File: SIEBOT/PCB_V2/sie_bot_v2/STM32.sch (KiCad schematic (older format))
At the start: 23 parts, among them U10 STM32F105RC, X3 8 MHz

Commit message: Adición de programadores con ejemplos de manejo de los diferentes periféricos
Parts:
- removed X3: 8 MHz, symbol CRYSTAL
- added X3: 8MHz, ABM8G, symbol ABM8G
- C26, C28, C33, C55, C58, C72, D10, D8, D9, R26, R27, R33, R34, R35, R5: footprint (none) -> SM0603
- C54, C73: footprint (none) -> SM0805
- C56: value 1uF -> 0.1uF; footprint (none) -> SM0603
- C59: footprint (none) -> SM1206
- U10: footprint lqfp64 -> TQFP_64
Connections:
- net labels removed: STM32_FP[0..40]
- wire segments 112 -> 116
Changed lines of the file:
@@
-EESchema Schematic File Version 2  date Tue 20 Sep 2011 03:35:58 PM COT
+EESchema Schematic File Version 2  date Wed 21 Sep 2011 02:34:46 PM COT
 LIBS:con-jack
 LIBS:adm3101e
@@
 Sheet 2 5
 Title ""
-Date "20 sep 2011"
+Date "21 sep 2011"
 Rev ""
 Comp ""
@@
 Comment4 ""
 $EndDescr
-Text Label 6000 2300 0    60   ~ 0
-STM32_FP42
-Text Label 6000 2200 0    60   ~ 0
-STM32_FP41
+Wire Wire Line
+	1000 2050 1000 2300
+Wire Wire Line
+	1000 2050 1150 2050
 Wire Bus Line
 	6750 4600 6750 2300
@@
 Wire Wire Line
 	6650 4400 5750 4400
+Wire Wire Line
+	1150 1950 1000 1950
+Wire Wire Line
+	1000 1950 1000 1700
+$Comp
+L ABM8G X3
+U 1 1 4E7A2D7B
+P 1550 2000
+F 0 "X3" H 1550 2150 60  0000 C CNN
+F 1 "8MHz" H 1550 1850 60  0000 C CNN
+F 2 "ABM8G" H 1550 2000 60  0001 C CNN
+	1    1550 2000
+	0    1    1    0
+$EndComp
+Text Label 6000 2300 0    60   ~ 0
+STM32_FP42
+Text Label 6000 2200 0    60   ~ 0
+STM32_FP41
 Entry Wire Line
 	6650 2200 6750 2300
@@
 F 0 "R27" V 9580 4550 50  0000 C CNN
 F 1 "10k" V 9500 4550 50  0000 C CNN
+F 2 "SM0603" H 9500 4550 60  0001 C CNN
 	1    9500 4550
 	-1   0    0    1
@@
 El procesador selecciona si inicia por \nla flash o ram internas.\nSe debe soldar solo R26 o R34\n\n
 $Comp
-L GND #PWR13
+L GND #PWR01
 U 1 1 4E78C5F4
 P 10450 4900
-F 0 "#PWR13" H 10450 4900 30  0001 C CNN
+F 0 "#PWR01" H 10450 4900 30  0001 C CNN
 F 1 "GND" H 10450 4830 30  0001 C CNN
 	1    10450 4900
@@
 F 0 "R26" V 9930 4550 50  0000 C CNN
 F 1 "510" V 9850 4550 50  0000 C CNN
+F 2 "SM0603" H 9850 4550 60  0001 C CNN
 	1    9850 4550
 	-1   0    0    1
@@
 F 0 "R34" V 10530 4550 50  0000 C CNN
 F 1 "10k" V 10450 4550 50  0000 C CNN
+F 2 "SM0603" H 10450 4550 60  0001 C CNN
 	1    10450 4550
 	-1   0    0    1
@@
 $EndComp
 $Comp
-L GND #PWR5
+L GND #PWR02
 U 1 1 4E78C2ED
 P 5300 7400
-F 0 "#PWR5" H 5300 7400 30  0001 C CNN
+F 0 "#PWR02" H 5300 7400 30  0001 C CNN
 F 1 "GND" H 5300 7330 30  0001 C CNN
 	1    5300 7400
@@
 F 0 "C59" H 10450 2550 50  0000 L CNN
 F 1 "10uF Tant." H 10450 2350 50  0000 L CNN
+F 2 "SM1206" H 10400 2450 60  0001 C CNN
 	1    10400 2450
 	1    0    0    -1
@@
 STM32_FP17
 $Comp
-L GND #PWR16
+L GND #PWR03
 U 1 1 4E188E68
 P 10950 1500
-F 0 "#PWR16" H 10950 1500 30  0001 C CNN
+F 0 "#PWR03" H 10950 1500 30  0001 C CNN
 F 1 "GND" H 10950 1430 30  0001 C CNN
 	1    10950 1500
@@
 F 0 "D10" H 10550 1300 50  0000 C CNN
 F 1 "LED" H 10550 1100 50  0000 C CNN
+F 2 "SM0603" H 10550 1200 60  0001 C CNN
 	1    10550 1200
 	-1   0    0    1
@@
 F 0 "R35" V 10630 1500 50  0000 C CNN
 F 1 "1k" V 10550 1500 50  0000 C CNN
+F 2 "SM0603" H 10550 1500 60  0001 C CNN
 	1    10550 1500
 	0    1    1    0
@@
 F 0 "R33" V 9780 1500 50  0000 C CNN
 F 1 "1k" V 9700 1500 50  0000 C CNN
+F 2 "SM0603" H 9700 1500 60  0001 C CNN
 	1    9700 1500
 	0    1    1    0
@@
 F 0 "D9" H 9700 1300 50  0000 C CNN
 F 1 "LED" H 9700 1100 50  0000 C CNN
+F 2 "SM0603" H 9700 1200 60  0001 C CNN
 	1    9700 1200
 	-1   0    0    1
 $EndComp
 $Comp
-L GND #PWR11
+L GND #PWR04
 U 1 1 4E188E4E
 P 10100 1500
-F 0 "#PWR11" H 10100 1500 30  0001 C CNN
+F 0 "#PWR04" H 10100 1500 30  0001 C CNN
 F 1 "GND" H 10100 1430 30  0001 C CNN
 	1    10100 1500
@@
 STM32_FP1
 $Comp
-L GND #PWR7
+L GND #PWR05
 U 1 1 4E186DEB
 P 9250 1500
-F 0 "#PWR7" H 9250 1500 30  0001 C CNN
+F 0 "#PWR05" H 9250 1500 30  0001 C CNN
 F 1 "GND" H 9250 1430 30  0001 C CNN
 	1    9250 1500
@@
 F 0 "U10" H 3200 8150 60  0000 C CNN
 F 1 "STM32F105RC" H 5100 2600 60  0000 C CNN
-F 2 "lqfp64" H 3140 8210 60  0001 C CNN
+F 2 "TQFP_64" H 3140 8210 60  0001 C CNN
 	1    4200 4800
 	1    0    0    -1
@@
 P 9700 2450
 F 0 "C56" H 9750 2550 50  0000 L CNN
-F 1 "1uF" H 9750 2350 50  0000 L CNN
+F 1 "0.1uF" H 9750 2350 50  0000 L CNN
+F 2 "SM0603" H 9700 2450 60  0001 C CNN
 	1    9700 2450
 	1    0    0    -1
@@
 F 0 "C54" H 9050 2550 50  0000 L CNN
 F 1 "1uF" H 9050 2350 50  0000 L CNN
+F 2 "SM0805" H 9000 2450 60  0001 C CNN
 	1    9000 2450
 	1    0    0    -1
 $EndComp
 $Comp
-L GND #PWR14
+L GND #PWR06
 U 1 1 4E07869F
 P 10600 2750
-F 0 "#PWR14" H 10600 2750 30  0001 C CNN
+F 0 "#PWR06" H 10600 2750 30  0001 C CNN
 F 1 "GND" H 10600 2680 30  0001 C CNN
 	1    10600 2750
@@
 $EndComp
 $Comp
-L GND #PWR3
+L GND #PWR07
 U 1 1 4DCDB18D
 P 4300 7400
-F 0 "#PWR3" H 4300 7400 30  0001 C CNN
+F 0 "#PWR07" H 4300 7400 30  0001 C CNN
 F 1 "GND" H 4300 7330 30  0001 C CNN
 	1    4300 7400
@@
 F 0 "C33" H 8700 2550 50  0000 L CNN
 F 1 "0.1uF" H 8700 2350 50  0000 L CNN
+F 2 "SM0603" H 8650 2450 60  0001 C CNN
 	1    8650 2450
 	1    0    0    -1
@@
 F 0 "C55" H 9400 2550 50  0000 L CNN
 F 1 "0.1uF" H 9400 2350 50  0000 L CNN
+F 2 "SM0603" H 9350 2450 60  0001 C CNN
 	1    9350 2450
 	1    0    0    -1
@@
 F 0 "C58" H 10100 2550 50  0000 L CNN
 F 1 "0.1uF" H 10100 2350 50  0000 L CNN
+F 2 "SM0603" H 10050 2450 60  0001 C CNN
 	1    10050 2450
 	1    0    0    -1
@@
 F 0 "C72" H 10450 3400 50  0000 L CNN
 F 1 "0.1uF" H 10450 3200 50  0000 L CNN
+F 2 "SM0603" H 10400 3300 60  0001 C CNN
 	1    10400 3300
 	1    0    0    -1
@@
 F 0 "C73" H 10850 3400 50  0000 L CNN
 F 1 "1uF" H 10850 3200 50  0000 L CNN
+F 2 "SM0805" H 10800 3300 60  0001 C CNN
 	1    10800 3300
 	1    0    0    -1
 $EndComp
 $Comp
-L GND #PWR15
+L GND #PWR08
 U 1 1 4DCDB183
 P 10600 3600
-F 0 "#PWR15" H 10600 3600 30  0001 C CNN
+F 0 "#PWR08" H 10600 3600 30  0001 C CNN
 F 1 "GND" H 10600 3530 30  0001 C CNN
 	1    10600 3600
@@
 NRST
 $Comp
-L GND #PWR1
+L GND #PWR09
 U 1 1 4DCDB180
 P 700 2050
-F 0 "#PWR1" H 700 2050 30  0001 C CNN
+F 0 "#PWR09" H 700 2050 30  0001 C CNN
 F 1 "GND" H 700 1980 30  0001 C CNN
 	1    700  2050
 	-1   0    0    -1
-$EndComp
-$Comp
-L CRYSTAL X3
-U 1 1 4DCDB17F
-P 1550 2000
-F 0 "X3" H 1650 2150 60  0000 C CNN
-F 1 "8 MHz" H 1550 1850 60  0000 C CNN
-	1    1550 2000
-	0    -1   1    0
 $EndComp
 Text Label 2500 1800 0    60   ~ 0
@@
 BOOT0
 $Comp
-L GND #PWR9
+L GND #PWR010
 U 1 1 4DCDB17D
 P 9500 4900
-F 0 "#PWR9" H 9500 4900 30  0001 C CNN
+F 0 "#PWR010" H 9500 4900 30  0001 C CNN
 F 1 "GND" H 9500 4830 30  0001 C CNN
 	1    9500 4900
@@
 	850  4050 950  4150
 Text HLabel 1400 4350 2    60   BiDi ~ 0
-STM32_FP[0..40]
+STM32_FP[0..42]
 Text Label 1000 2650 0    60   ~ 0
 STM32_FP0
@@
 F 0 "D8" H 8850 1300 50  0000 C CNN
 F 1 "LED" H 8850 1100 50  0000 C CNN
+F 2 "SM0603" H 8850 1200 60  0001 C CNN
 	1    8850 1200
 	-1   0    0    1
@@
 F 0 "R5" V 8930 1500 50  0000 C CNN
 F 1 "1k" V 8850 1500 50  0000 C CNN
+F 2 "SM0603" H 8850 1500 60  0001 C CNN
 	1    8850 1500
 	0    1    1    0
@@
 F 0 "C26" H 1250 1800 50  0000 L CNN
 F 1 "22pF" H 1250 1600 50  0000 L CNN
+F 2 "SM0603" H 1200 1700 60  0001 C CNN
 	1    1200 1700
 	0    1    1    0
@@
 F 0 "C28" H 1250 2400 50  0000 L CNN
 F 1 "22pF" H 1250 2200 50  0000 L CNN
+F 2 "SM0603" H 1200 2300 60  0001 C CNN
 	1    1200 2300
 	0    1    1    0

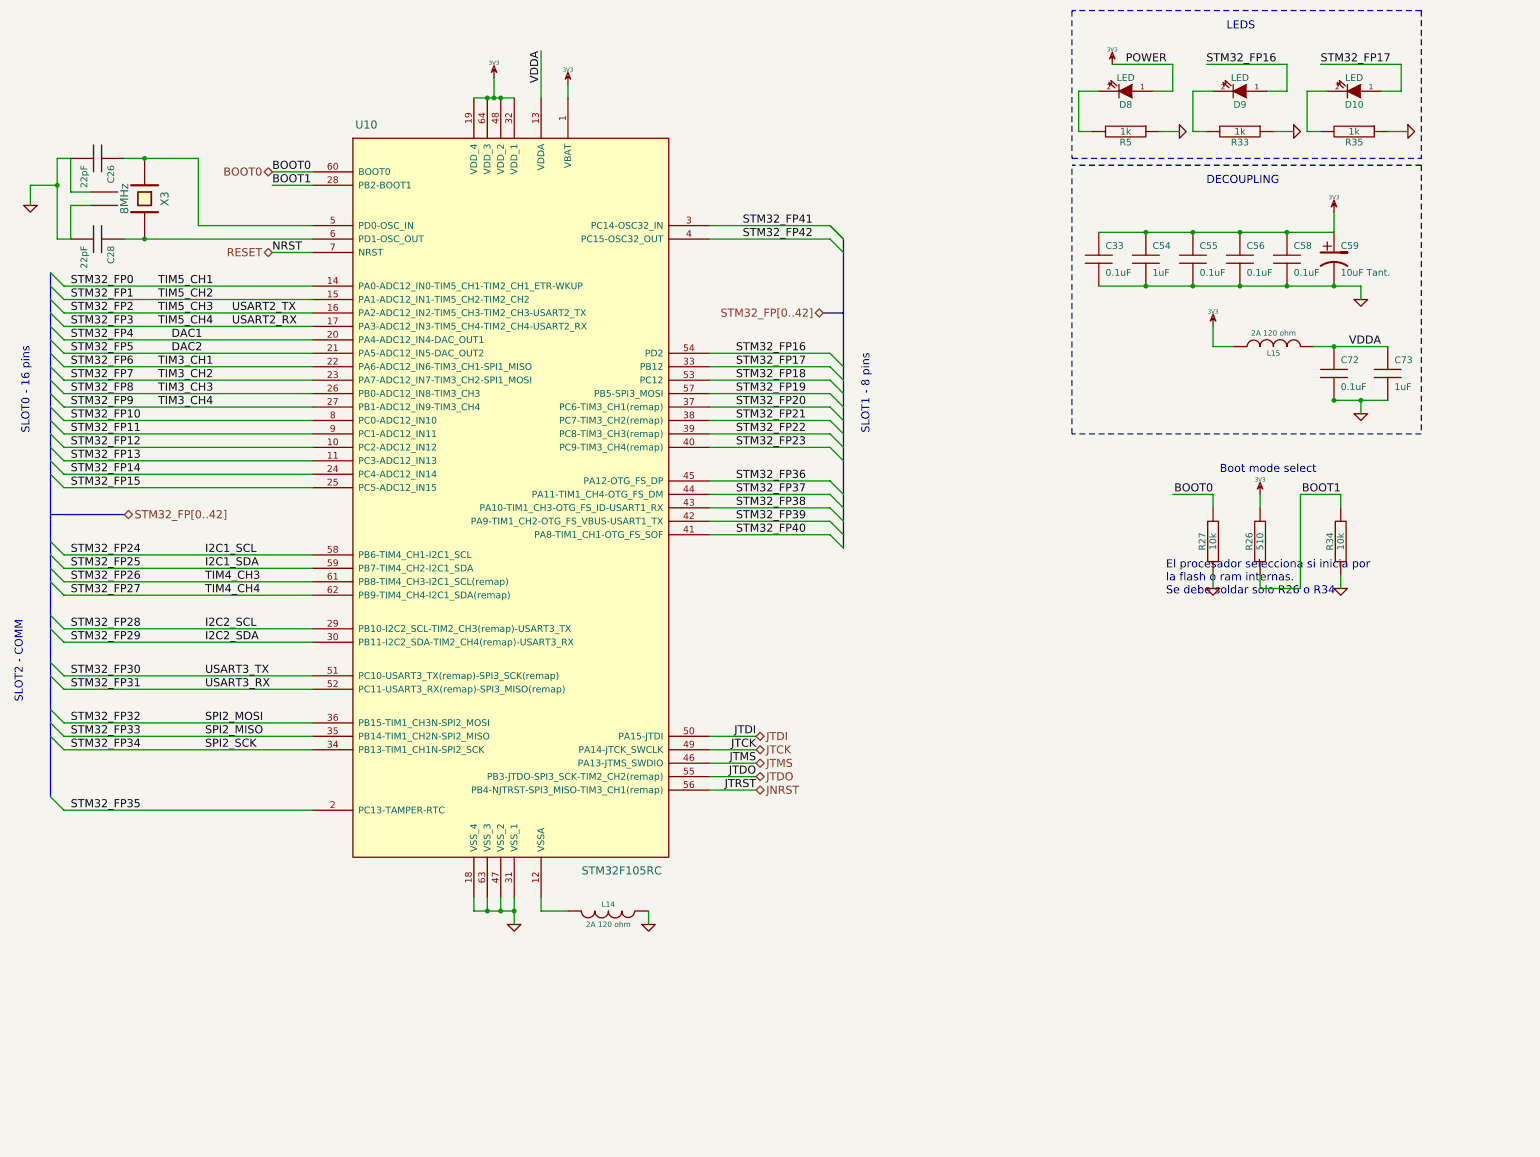
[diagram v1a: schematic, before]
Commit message: Conexión del STM32 con el procesador, adición de un regulador de 3.3V disponible para el usuario
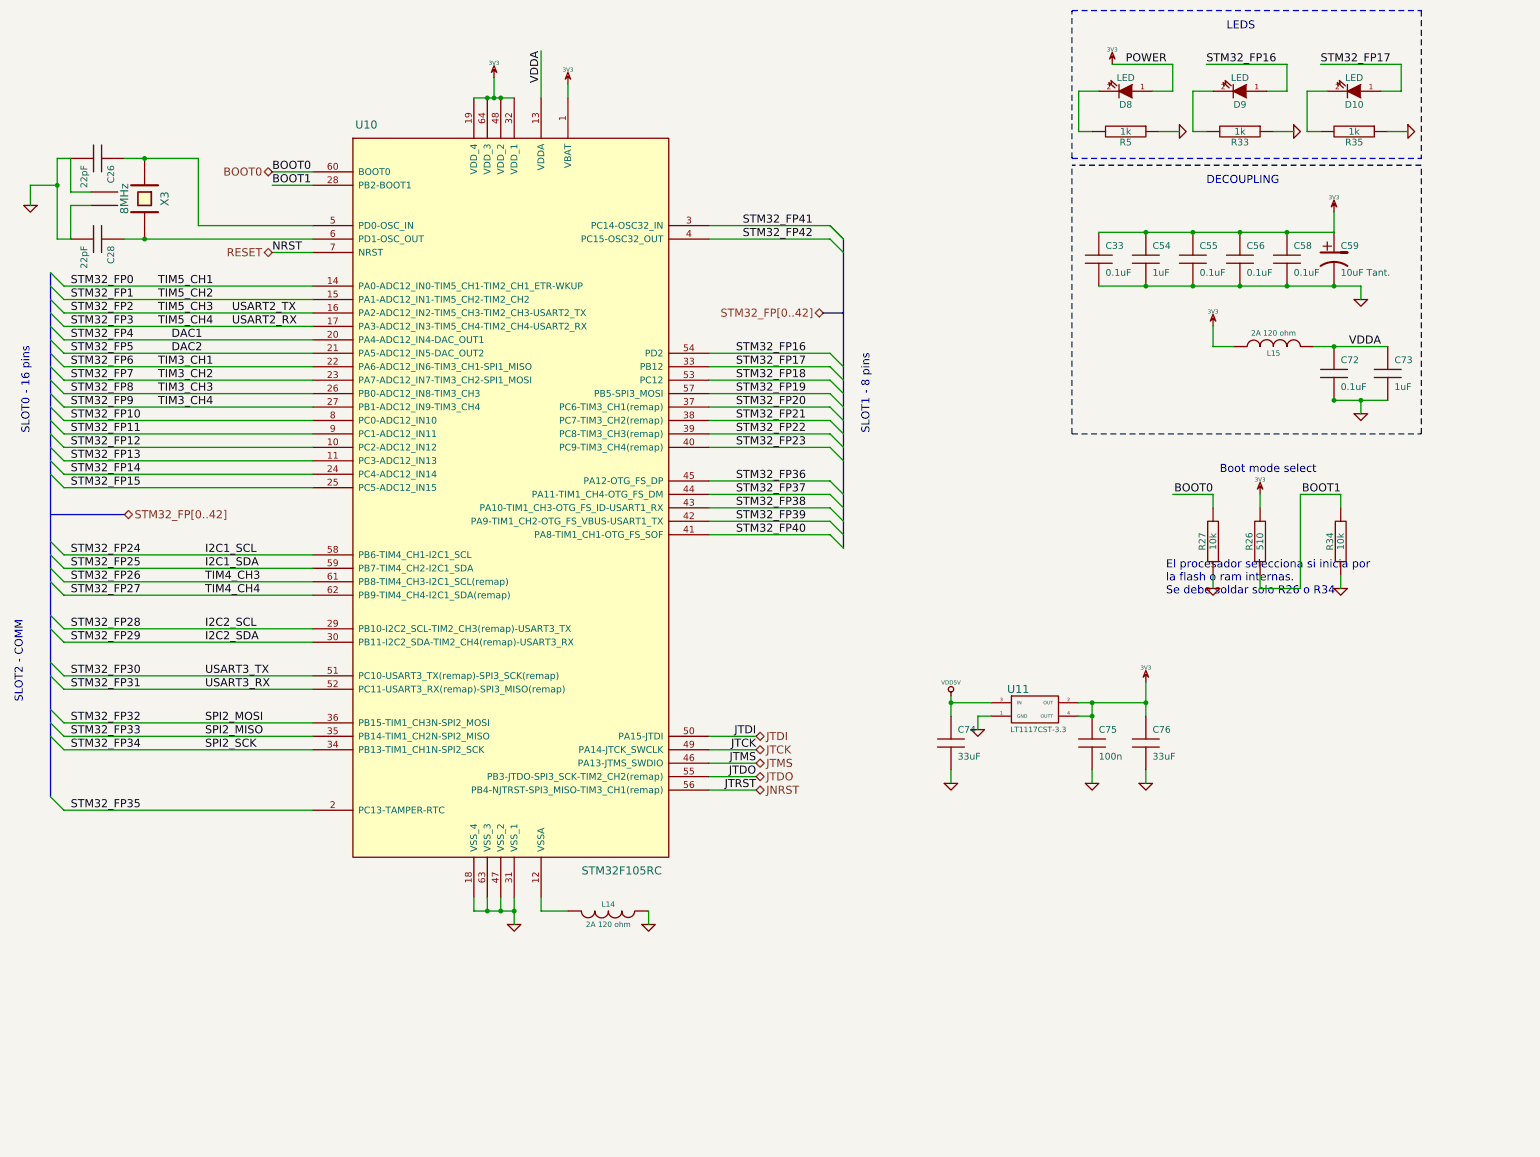
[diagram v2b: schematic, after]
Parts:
- added C74, C76: 33uF, SM1206, symbol C
- added C75: 100n, SM0603, symbol C
- added U11: LT1117CST-3.3, LT1117, symbol LT1117CST
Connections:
- net 3V3: now also C75.1, C76.1, U11.2 (OUT), U11.4 (OUTT)
- net GND: now also C74.2, C75.2, C76.2, U11.1 (GND)
- new net VDD5V: C74.1, U11.3 (IN)

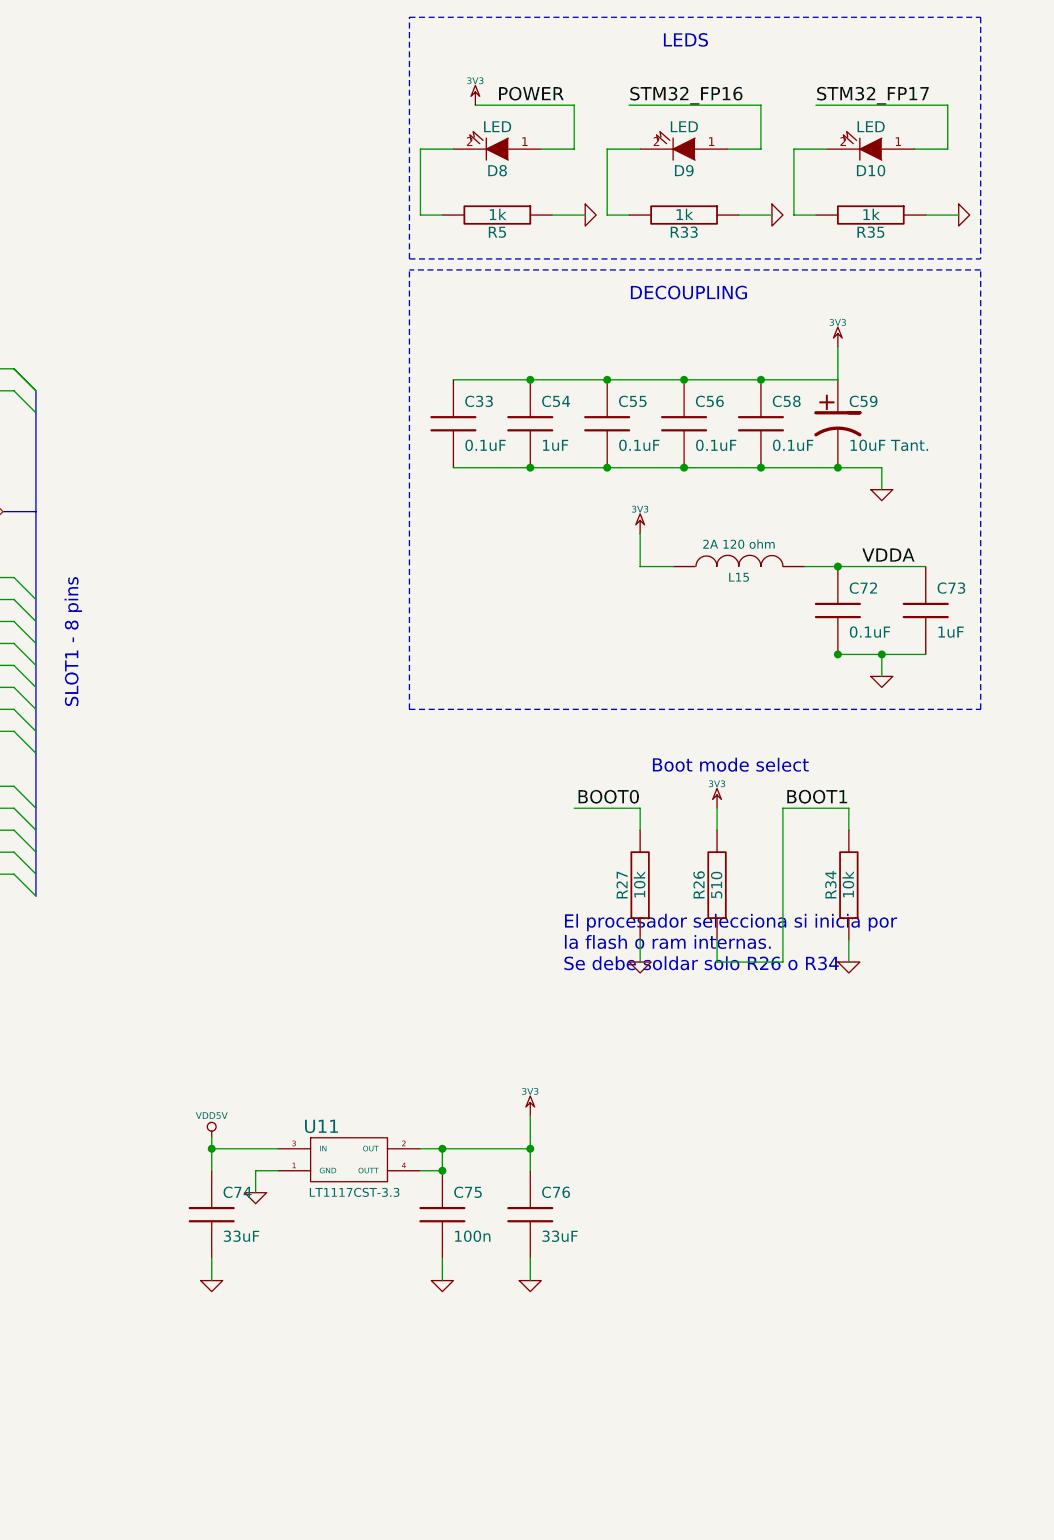
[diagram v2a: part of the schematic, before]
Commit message: Ruteo de la conexión entre el procesador y el STM32, re-localización de los conectores de alimentación y USB, adidición del regulador de 3.3V
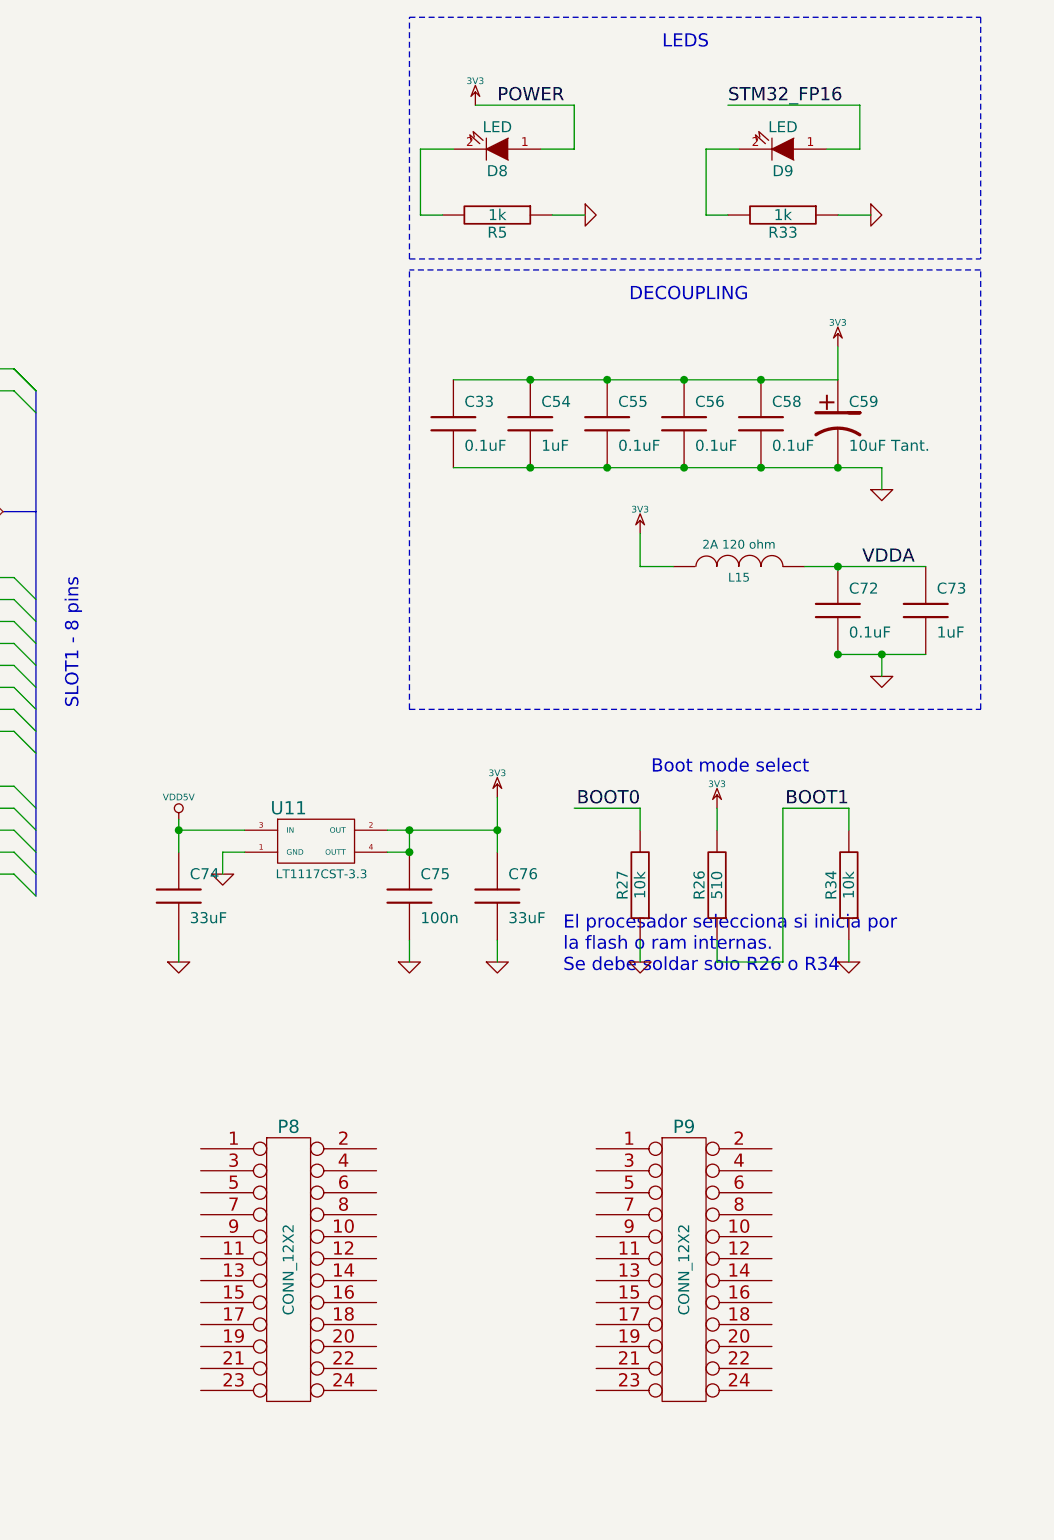
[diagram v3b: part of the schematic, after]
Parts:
- removed D10: LED, SM0603, symbol LED
- removed R35: 1k, SM0603, symbol R
- added P8, P9: CONN_12X2, pin_array_12x2, symbol CONN_12X2
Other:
- moved on the sheet: C74, C75, C76, D9, R33, U11
